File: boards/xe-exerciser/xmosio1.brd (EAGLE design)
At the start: 108 x 69.8 mm, 9 parts, among them J1 POWER_JACKPTH

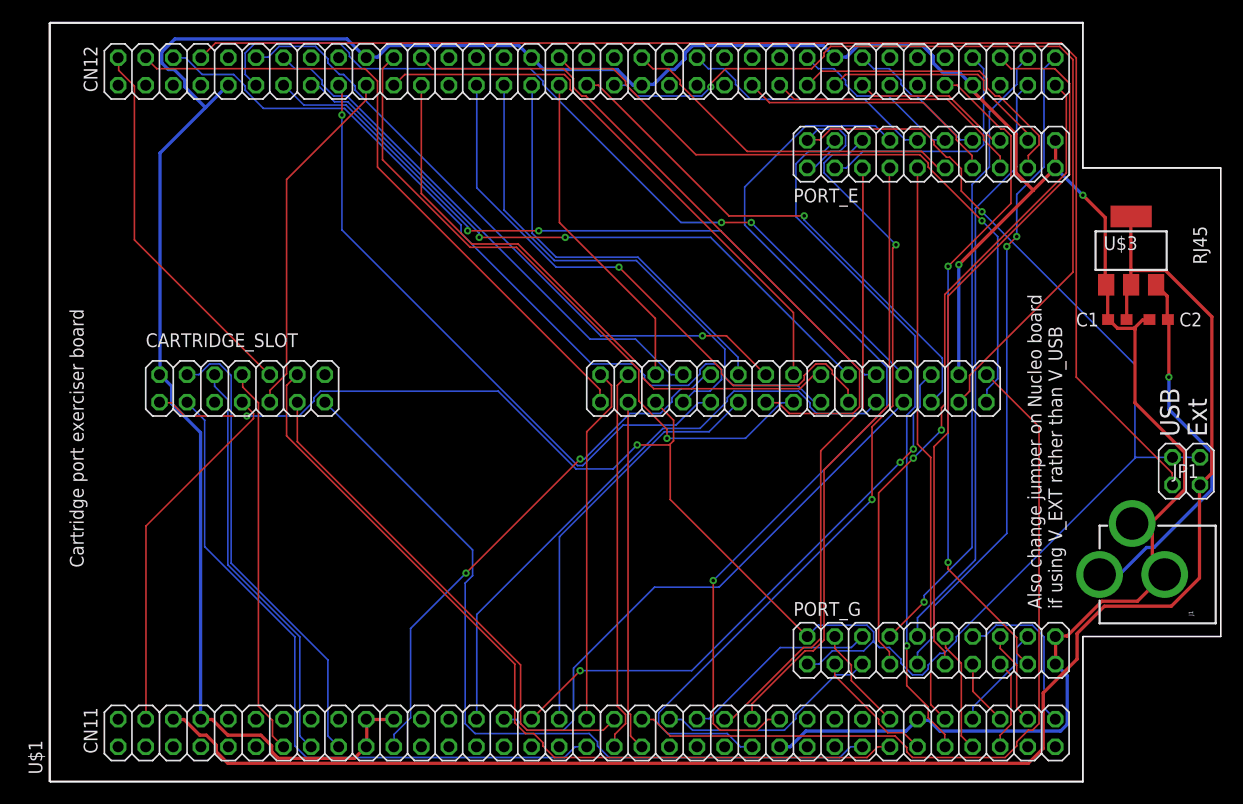
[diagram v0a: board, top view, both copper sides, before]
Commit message: Use the correct pinouts for the ECI/cartridge port harness
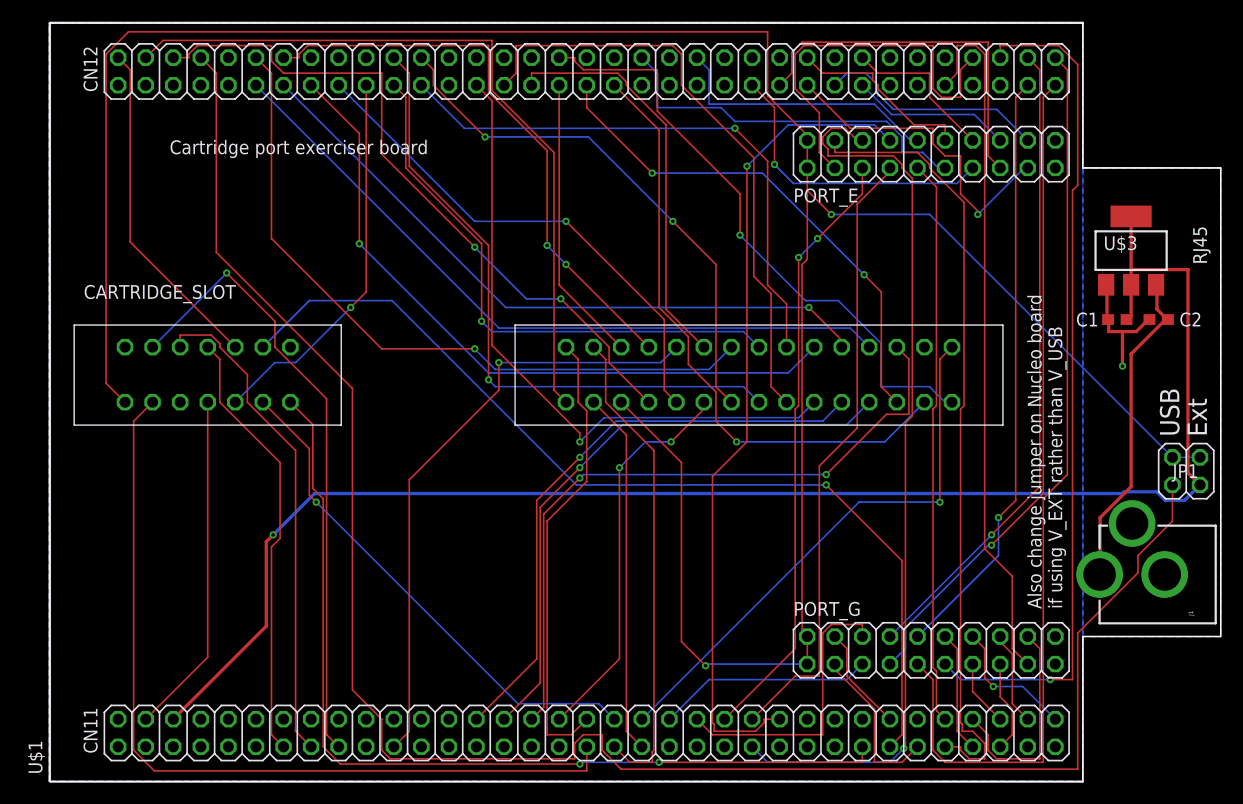
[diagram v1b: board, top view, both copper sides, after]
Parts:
- moved CARTRIDGE_SLOT 8.35 mm to (41.3, 38.1)
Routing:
- net GND: track 312.1 -> 11.9 mm, vias 2 -> 1
- net N$2: track 124.8 -> 168.9 mm
- net +5V: track 194.4 -> 238.1 mm, vias 3 -> 2
- net A3: track 81.4 -> 56.3 mm
- net N$25: track 61.2 -> 85.5 mm, vias 2 -> 0
- net BK_EN_LO: track 74.0 -> 50.5 mm, vias 0 -> 1
- net D1: track 65.6 -> 49.2 mm, vias 0 -> 2
- net A15: track 43.2 -> 57.6 mm, vias 0 -> 1
- net !REFRESH!: track 63.5 -> 77.6 mm
- net N$3: track 23.0 -> 36.0 mm
- net D6: track 58.9 -> 47.0 mm
- net N$26: track 66.5 -> 78.2 mm, vias 0 -> 1
- net A5: track 77.5 -> 66.5 mm, vias 2 -> 0
- net !EXTSEL!: track 74.1 -> 84.8 mm, vias 0 -> 2
- net N$34: track 9.72 -> 20.3 mm
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- added copper zone on layer 16, net GND
